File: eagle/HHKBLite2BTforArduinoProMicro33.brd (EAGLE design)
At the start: 100 x 61 mm, 40 parts, among them CON1 45045-1445, CON2 45045-0845, IC1 4514N, IC2 4512N, IC4 HT7733A, J1 J7MM, J2 J15MM, J3 J7MM, J4 J10MM

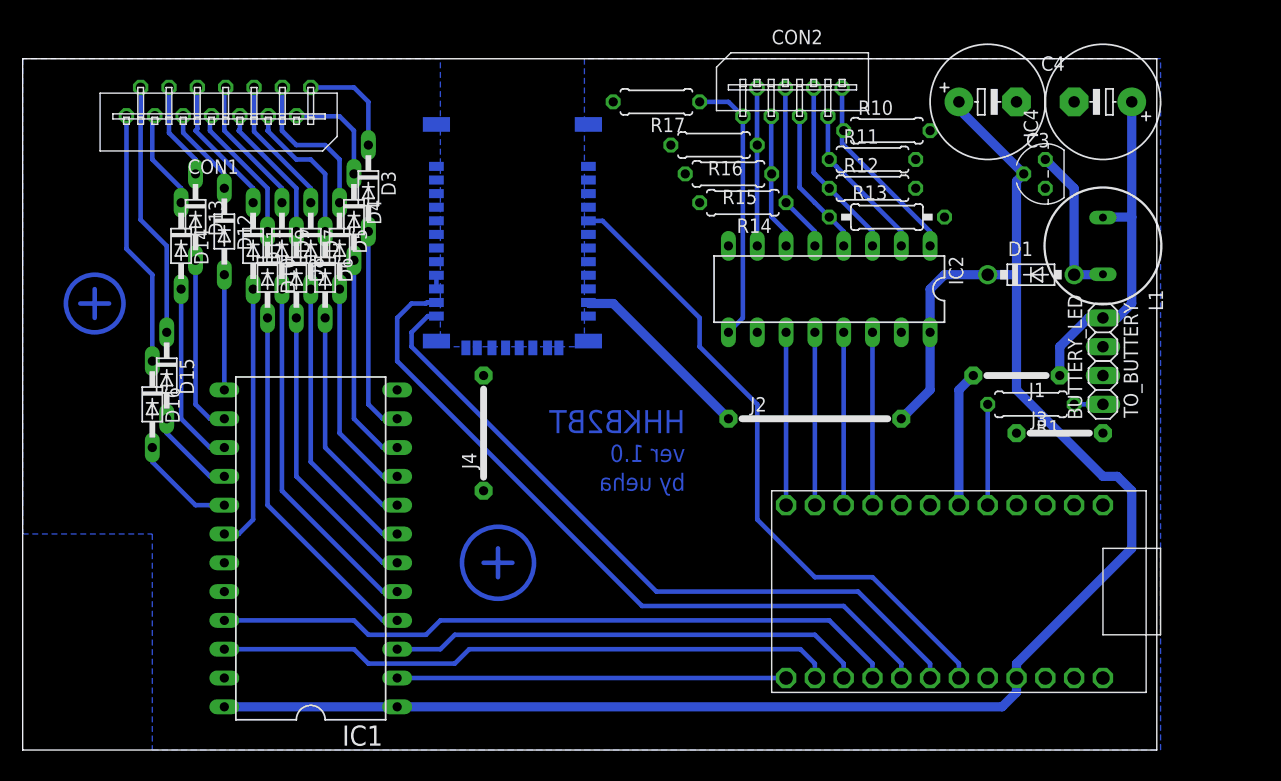
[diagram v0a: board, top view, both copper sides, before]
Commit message: いろいろ変えた
回路図については, 電源周りとかアライメントとかを調節した.
また, パーツのサイズを, 実際に使いそうなサイズにフィットさせた.
プログラムは移動させた.
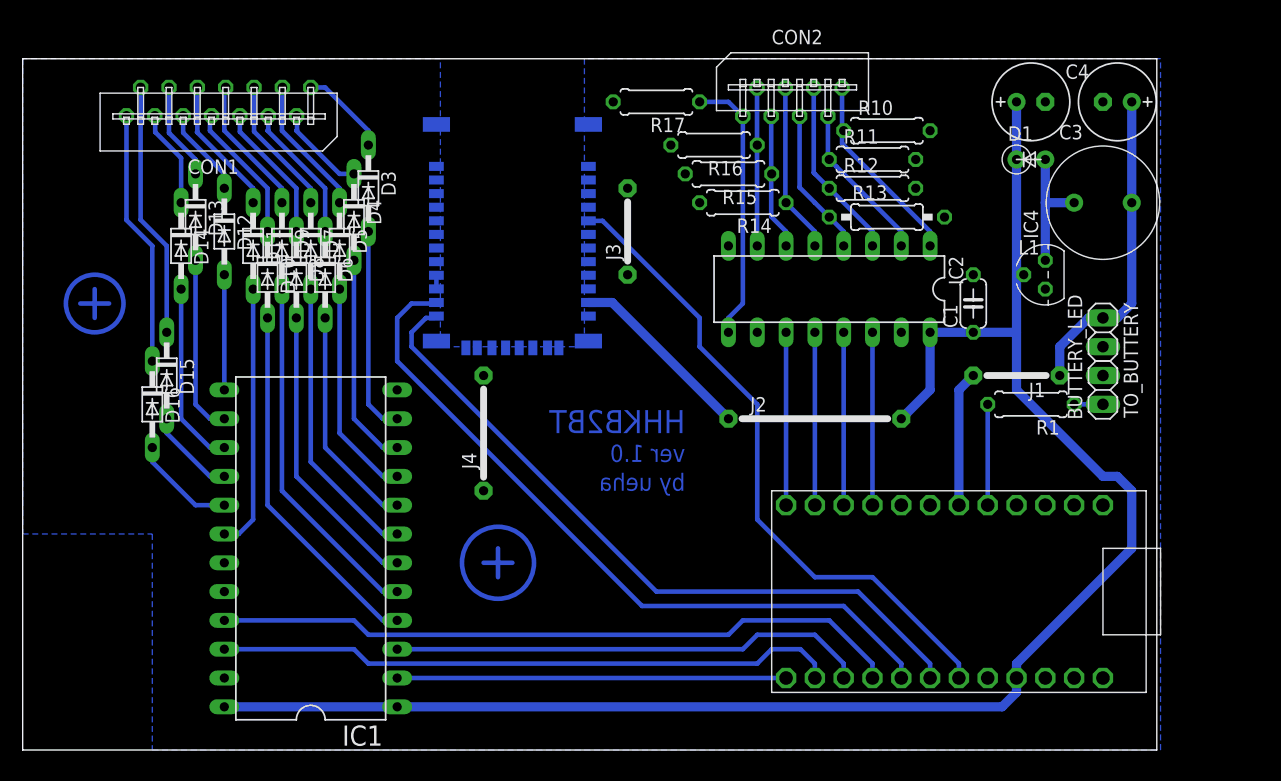
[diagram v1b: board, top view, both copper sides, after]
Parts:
- added C1: 0.1uF, rcl:C050-024X044
- C3: device rcl:E5-10,5 -> rcl:E2,5-7
- C4: value 22uF -> 100uF; device rcl:E5-10,5 -> rcl:E2,5-7
- D1: value 1N5817-B -> SCHOTTKY-DIODEDOWN; device diode:DO41-7.6 -> MySilicon:DIODE-STAND-DOWN
- L1: value 47uH -> 100uH; device inductor-neosid:BS11 -> MyRCL:E5-10
- R1: value 330 -> 160
- moved J3 42.0 mm to (53.3, 45.7), turned to 90 degrees
- moved D1 10.2 mm to (88.9, 52.1)
- moved IC4 8.89 mm to (90.2, 41.9)
- moved C4 3.81 mm to (88.9, 57.1)
- moved L1 3.81 mm to (95.2, 48.3), turned to 180 degrees
- moved C3 1.27 mm to (96.5, 57.1)
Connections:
- removed net N$10: J2.1, U$1.11
- removed net N$8: J1.2, U$2.7
- net +3V3: now also C1.1, J2.1, U$1.11
- net GND: now also C1.2
- net N$3: now also L1.+1; no longer L1.2
- net N$4: now also J1.2, L1.+, U$2.7; no longer L1.1
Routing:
- net N$10: track 16.6 -> 0.00 mm
- net N$8: track 12.0 -> 0.00 mm
- net +3V3: track 154.9 -> 165.1 mm
- net N$4: track 30.8 -> 40.2 mm
- net N$3: track 13.8 -> 11.4 mm
- net N$51: track 13.8 -> 12.3 mm
- net N$49: track 9.42 -> 7.93 mm
- net N$50: track 9.41 -> 8.01 mm
- net N$52: track 13.1 -> 12.3 mm

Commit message: ProMicro33用コードと回路図を変更
各ICとのピンの番号が整合するように調節した.
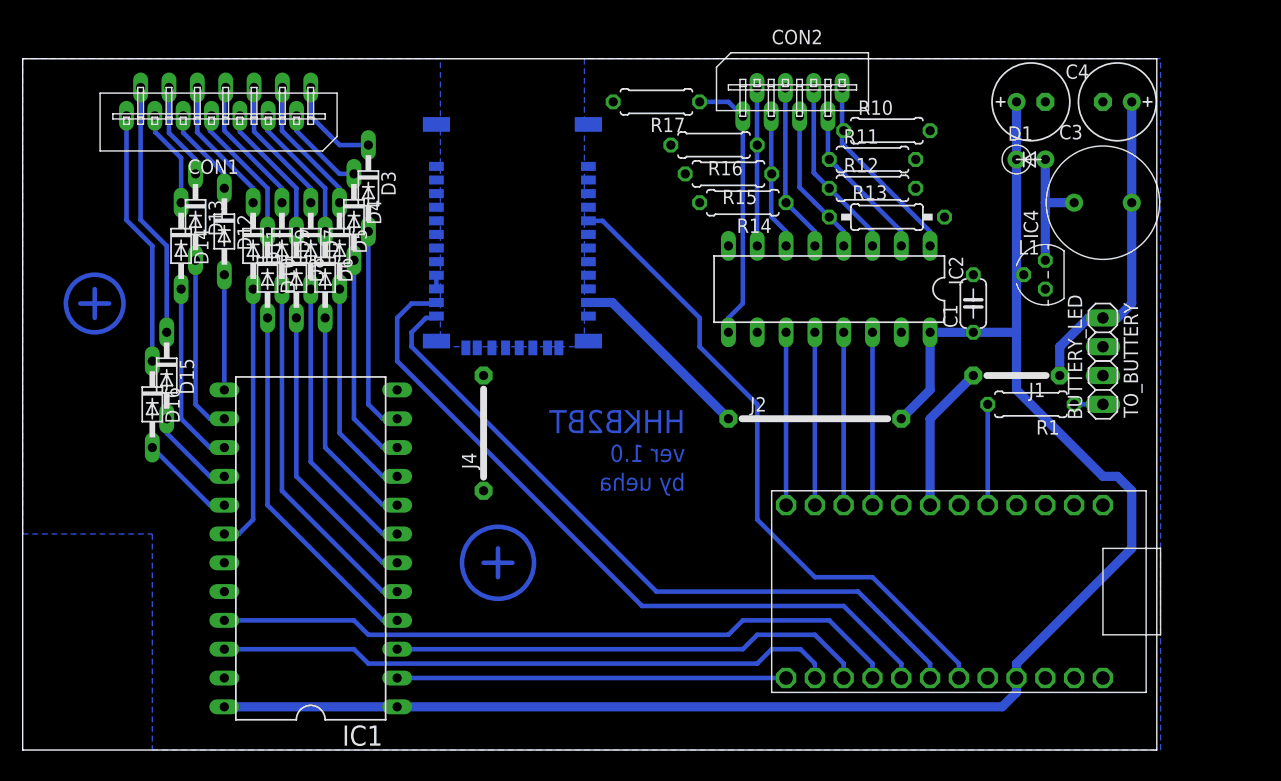
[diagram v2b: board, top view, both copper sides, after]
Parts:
- removed J3: J7MM, jumper:07
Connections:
- removed net N$4: C3.+, J1.1, J1.2, L1.+, TO_BUTTERY.1, U$2.7
- new net VCC_SRC: C3.+, J1.1, J1.2, L1.+, TO_BUTTERY.1, U$2.6
- net GND: no longer J3.1, J3.2
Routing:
- net VCC_SRC: track 0.00 -> 41.3 mm
- net N$4: track 40.2 -> 0.00 mm
- net CON1BUS_O9: track 10.5 -> 8.45 mm
- net N$49: track 7.93 -> 8.67 mm
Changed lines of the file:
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@@
 <setting verticaltext="up"/>
 </settings>
-<grid distance="0.05" unitdist="inch" unit="inch" style="lines" multiple="1" display="yes" altdistance="0.025" altunitdist="inch" altunit="inch"/>
+<grid distance="0.05" unitdist="inch" unit="mil" style="lines" multiple="1" display="yes" altdistance="0.025" altunitdist="inch" altunit="inch"/>
 <layers>
-<layer number="1" name="Top" color="4" fill="1" visible="no" active="yes"/>
+<layer number="1" name="Top" color="4" fill="1" visible="yes" active="yes"/>
 <layer number="16" name="Bottom" color="1" fill="1" visible="yes" active="yes"/>
 <layer number="17" name="Pads" color="2" fill="1" visible="yes" active="yes"/>
@@
 <layer number="37" name="tTest" color="7" fill="1" visible="no" active="yes"/>
 <layer number="38" name="bTest" color="7" fill="1" visible="no" active="yes"/>
-<layer number="39" name="tKeepout" color="4" fill="11" visible="yes" active="yes"/>
-<layer number="40" name="bKeepout" color="1" fill="11" visible="yes" active="yes"/>
-<layer number="41" name="tRestrict" color="4" fill="10" visible="yes" active="yes"/>
-<layer number="42" name="bRestrict" color="1" fill="10" visible="yes" active="yes"/>
-<layer number="43" name="vRestrict" color="2" fill="10" visible="yes" active="yes"/>
-<layer number="44" name="Drills" color="7" fill="1" visible="yes" active="yes"/>
-<layer number="45" name="Holes" color="7" fill="1" visible="yes" active="yes"/>
+<layer number="39" name="tKeepout" color="4" fill="11" visible="no" active="yes"/>
+<layer number="40" name="bKeepout" color="1" fill="11" visible="no" active="yes"/>
+<layer number="41" name="tRestrict" color="4" fill="10" visible="no" active="yes"/>
+<layer number="42" name="bRestrict" color="1" fill="10" visible="no" active="yes"/>
+<layer number="43" name="vRestrict" color="2" fill="10" visible="no" active="yes"/>
+<layer number="44" name="Drills" color="7" fill="1" visible="no" active="yes"/>
+<layer number="45" name="Holes" color="7" fill="1" visible="no" active="yes"/>
 <layer number="46" name="Milling" color="3" fill="1" visible="no" active="yes"/>
 <layer number="47" name="Measures" color="7" fill="1" visible="no" active="yes"/>
 <layer number="48" name="Document" color="7" fill="1" visible="no" active="yes"/>
 <layer number="49" name="Reference" color="7" fill="1" visible="no" active="yes"/>
-<layer number="51" name="tDocu" color="7" fill="1" visible="no" active="yes"/>
-<layer number="52" name="bDocu" color="7" fill="1" visible="no" active="yes"/>
+<layer number="51" name="tDocu" color="7" fill="1" visible="yes" active="yes"/>
+<layer number="52" name="bDocu" color="7" fill="1" visible="yes" active="yes"/>
 <layer number="90" name="Modules" color="5" fill="1" visible="no" active="no"/>
 <layer number="91" name="Nets" color="2" fill="1" visible="no" active="no"/>
@@
 </class>
 <class number="1" name="Vcc" width="0.0254" drill="0">
-<clearance class="0" value="0.508"/>
+<clearance class="1" value="0.205"/>
 </class>
 <class number="2" name="VccSrc" width="0" drill="0">
-<clearance class="0" value="0.508"/>
-<clearance class="1" value="0.508"/>
 <clearance class="2" value="0.508"/>
 </class>
 <class number="3" name="GND" width="0" drill="0">
-<clearance class="0" value="0.3048"/>
 <clearance class="1" value="0.508"/>
 <clearance class="2" value="0.508"/>
+<clearance class="3" value="0.205"/>
 </class>
 </classes>
-<designrules name="default">
+<designrules name="HHKBLite2BTforArduinoProMicro33 *">
 <description language="de">&lt;b&gt;EAGLE Design Rules&lt;/b&gt;
 &lt;p&gt;
@@
 <param name="mtCopper" value="0.035mm 0.035mm 0.035mm 0.035mm 0.035mm 0.035mm 0.035mm 0.035mm 0.035mm 0.035mm 0.035mm 0.035mm 0.035mm 0.035mm 0.035mm 0.035mm"/>
 <param name="mtIsolate" value="1.5mm 0.15mm 0.2mm 0.15mm 0.2mm 0.15mm 0.2mm 0.15mm 0.2mm 0.15mm 0.2mm 0.15mm 0.2mm 0.15mm 0.2mm"/>
-<param name="mdWireWire" value="8mil"/>
-<param name="mdWirePad" value="8mil"/>
-<param name="mdWireVia" value="8mil"/>
-<param name="mdPadPad" value="8mil"/>
-<param name="mdPadVia" value="8mil"/>
-<param name="mdViaVia" value="8mil"/>
+<param name="mdWireWire" value="0.205mm"/>
+<param name="mdWirePad" value="0.205mm"/>
+<param name="mdWireVia" value="0.205mm"/>
+<param name="mdPadPad" value="0.205mm"/>
+<param name="mdPadVia" value="0.205mm"/>
+<param name="mdViaVia" value="0.205mm"/>
 <param name="mdSmdPad" value="8mil"/>
 <param name="mdSmdVia" value="8mil"/>
@@
 <param name="mdViaViaSameLayer" value="8mil"/>
 <param name="mnLayersViaInSmd" value="2"/>
-<param name="mdCopperDimension" value="40mil"/>
+<param name="mdCopperDimension" value="0.2mm"/>
 <param name="mdDrill" value="8mil"/>
 <param name="mdSmdStop" value="0mil"/>
@@
 <element name="J4" library="jumper" package="10" value="J10MM" x="40.64" y="27.94" rot="R90"/>
 <element name="C1" library="rcl" package="C050-024X044" value="0.1uF" x="83.82" y="39.37" rot="R90"/>
-<element name="J3" library="jumper" package="07" value="J7MM" x="53.34" y="45.72" rot="R90"/>
 </elements>
 <signals>
@@
 <contactref element="R11" pad="2"/>
 <contactref element="BUTTERY_LED" pad="2"/>
-<polygon width="0.4064" layer="16">
+<polygon width="0.4064" layer="16" isolate="0.254">
 <vertex x="0" y="19.05"/>
 <vertex x="11.43" y="19.05"/>
@@
 <contactref element="U$2" pad="14"/>
 <contactref element="C1" pad="2"/>
-<contactref element="J3" pad="1"/>
 <contactref element="J4" pad="1"/>
-<contactref element="J3" pad="2"/>
 <contactref element="J4" pad="2"/>
-<wire x1="53.34" y1="41.91" x2="53.34" y2="49.53" width="0" layer="19" extent="1-1"/>
 <wire x1="33.02" y1="31.75" x2="36.48" y2="36.06" width="0" layer="19" extent="16-16"/>
 </signal>
@@
 <wire x1="36.48" y1="41.86" x2="36.48" y2="40.66" width="0.4064" layer="16"/>
 </signal>
-<signal name="N$4" class="2">
+<signal name="VCC_SRC" class="2">
 <contactref element="C3" pad="+"/>
 <contactref element="TO_BUTTERY" pad="1"/>
@@
 <wire x1="97.79" y1="48.26" x2="97.79" y2="39.37" width="0.8128" layer="16"/>
 <contactref element="J1" pad="2"/>
-<contactref element="U$2" pad="7"/>
-<wire x1="83.82" y1="33.02" x2="82.55" y2="31.75" width="0.8128" layer="16"/>
-<wire x1="82.55" y1="31.75" x2="82.55" y2="21.59" width="0.8128" layer="16"/>
+<contactref element="U$2" pad="6"/>
 <wire x1="83.82" y1="33.02" x2="91.44" y2="33.02" width="0" layer="19" extent="1-1"/>
+<wire x1="83.82" y1="33.02" x2="80.01" y2="29.21" width="0.8128" layer="16"/>
+<wire x1="80.01" y1="29.21" x2="80.01" y2="21.59" width="0.8128" layer="16"/>
 </signal>
 <signal name="N$49">
 <contactref element="CON1" pad="1"/>
 <contactref element="D3" pad="C"/>
-<wire x1="25.4" y1="58.42" x2="26.67" y2="58.42" width="0.4064" layer="16"/>
-<wire x1="26.67" y1="58.42" x2="30.48" y2="54.61" width="0.4064" layer="16"/>
-<wire x1="30.48" y1="54.61" x2="30.48" y2="53.34" width="0.4064" layer="16"/>
+<wire x1="25.4" y1="58.42" x2="25.4" y2="55.88" width="0.4064" layer="16"/>
+<wire x1="25.4" y1="55.88" x2="27.94" y2="53.34" width="0.4064" layer="16"/>
+<wire x1="27.94" y1="53.34" x2="30.48" y2="53.34" width="0.4064" layer="16"/>
 </signal>
 <signal name="N$50">
@@
 <contactref element="IC1" pad="17"/>
 <contactref element="D16" pad="A"/>
-<wire x1="11.43" y1="26.67" x2="11.43" y2="25.4" width="0.4064" layer="16"/>
-<wire x1="16.51" y1="21.59" x2="17.78" y2="21.59" width="0.4064" layer="16"/>
-<wire x1="11.43" y1="25.4" x2="15.24" y2="21.59" width="0.4064" layer="16"/>
-<wire x1="15.24" y1="21.59" x2="17.78" y2="21.59" width="0.4064" layer="16"/>
+<wire x1="17.78" y1="21.59" x2="16.51" y2="21.59" width="0.4064" layer="16"/>
+<wire x1="16.51" y1="21.59" x2="11.43" y2="26.67" width="0.4064" layer="16"/>
 </signal>
 <signal name="CON1BUS_O12">
